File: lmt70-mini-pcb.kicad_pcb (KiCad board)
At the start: 4 copper layers, 7.8 x 8.4 mm, 3 parts, among them P1 CONN_01X04, U1 LMT70

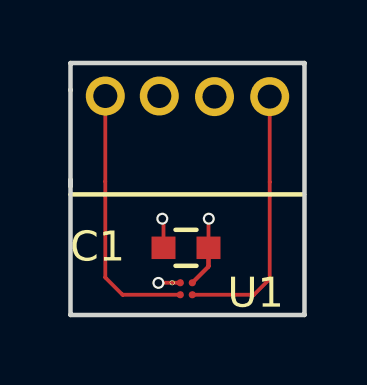
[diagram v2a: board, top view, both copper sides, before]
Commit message: PCB changed for manufacturing with JLCPCB
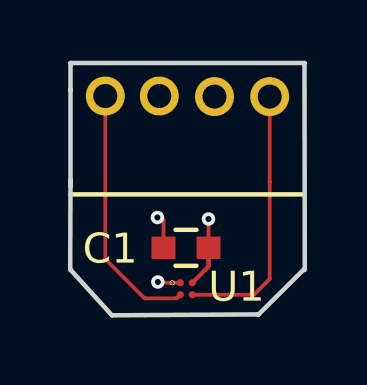
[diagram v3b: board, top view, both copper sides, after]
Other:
- outline, holes or cut-outs redrawn
- net class Default: via_dia 0.4 -> 0.45; via_drill 0.254 -> 0.2
- rule via_min_drill: 0.254 -> 0.2
- rule via_min_size: 0.4 -> 0.45
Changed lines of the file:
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@@
-(kicad_pcb (version 4) (host pcbnew 4.0.5)
+(kicad_pcb (version 20171130) (host pcbnew "(5.0.0-3-g5ebb6b6)")
   (general
-    (links 6)
-    (no_connects 0)
-    (area 146.169667 102.996809 156.290001 113.375001)
     (thickness 1.6)
-    (drawings 7)
-    (tracks 32)
+    (drawings 9)
+    (tracks 39)
     (zones 0)
     (modules 3)
@@
     (segment_width 0.15)
     (edge_width 0.15)
-    (via_size 0.4)
-    (via_drill 0.254)
-    (via_min_size 0.4)
-    (via_min_drill 0.254)
+    (via_size 0.45)
+    (via_drill 0.2)
+    (via_min_size 0.45)
+    (via_min_drill 0.2)
     (uvia_size 0.3)
     (uvia_drill 0.1)
@@
     (visible_elements FFFEFFFF)
     (pcbplotparams
-      (layerselection 0x01008_00000000)
+      (layerselection 0x010a8_ffffffff)
       (usegerberextensions false)
+      (usegerberattributes false)
+      (usegerberadvancedattributes false)
+      (creategerberjobfile false)
       (excludeedgelayer true)
       (linewidth 0.100000)
@@
       (hpglpennumber 1)
       (hpglpenspeed 20)
-      (hpglpendiameter 15)
-      (hpglpenoverlay 2)
+      (hpglpendiameter 15.000000)
       (psnegative false)
       (psa4output false)
@@
       (drillshape 0)
       (scaleselection 1)
-      (outputdirectory ""))
+      (outputdirectory "gerbers/"))
   )
   (net 0 "")
@@
     (clearance 0.127)
     (trace_width 0.127)
-    (via_dia 0.4)
-    (via_drill 0.254)
+    (via_dia 0.45)
+    (via_drill 0.2)
     (uvia_dia 0.3)
     (uvia_drill 0.1)
@@
     (tags "capacitor 0603")
     (attr smd)
-    (fp_text reference C1 (at 2.95 0.04 180) (layer F.SilkS)
+    (fp_text reference C1 (at 2.53 -0.03 180) (layer F.SilkS)
       (effects (font (size 1 1) (thickness 0.15)))
     )
@@
   (module lmt70:LMT70 (layer F.Cu)
     (at 151.659524 112.225)
-    (fp_text reference U1 (at 2.510476 0.335 180) (layer F.SilkS)
+    (fp_text reference U1 (at 1.870476 0.135 180) (layer F.SilkS)
       (effects (font (size 1 1) (thickness 0.15)))
     )
@@
       (net 4 "Net-(P1-Pad4)"))
   )
-  (gr_line (start 148 113.3) (end 148 108.8) (angle 90) (layer Edge.Cuts) (width 0.15))
-  (gr_line (start 155.8 113.3) (end 148 113.3) (angle 90) (layer Edge.Cuts) (width 0.15))
-  (gr_line (start 155.8 104.9) (end 155.8 113.3) (angle 90) (layer Edge.Cuts) (width 0.15))
+  (gr_line (start 154.27 113.28) (end 149.38 113.31) (layer Edge.Cuts) (width 0.15))
+  (gr_line (start 155.79 111.77) (end 154.26 113.29) (layer Edge.Cuts) (width 0.15))
+  (gr_line (start 149.38 113.31) (end 148 111.79) (layer Edge.Cuts) (width 0.15))
+  (gr_line (start 147.99 111.8) (end 148 108.8) (angle 90) (layer Edge.Cuts) (width 0.15))
+  (gr_line (start 155.8 104.9) (end 155.81 111.8) (angle 90) (layer Edge.Cuts) (width 0.15))
   (gr_line (start 148 104.9) (end 155.8 104.9) (angle 90) (layer Edge.Cuts) (width 0.15))
   (gr_line (start 148 105.8) (end 148 104.9) (angle 90) (layer Edge.Cuts) (width 0.15))
@@
   (gr_line (start 147.99 109.28) (end 155.79 109.28) (angle 90) (layer F.SilkS) (width 0.15))
   (segment (start 152.8 106.02) (end 152.8 108.87) (width 0.127) (layer In2.Cu) (net 1))
-  (segment (start 152.6 110.1) (end 152.6 111.684524) (width 0.127) (layer F.Cu) (net 1))
+  (segment (start 152.6 110.1) (end 152.6 110.1) (width 0.127) (layer F.Cu) (net 1))
   (segment (start 152.61 110.09) (end 152.6 110.1) (width 0.127) (layer F.Cu) (net 1))
-  (via (at 152.61 110.09) (size 0.4) (drill 0.254) (layers F.Cu B.Cu) (net 1))
   (segment (start 152.8 109.9) (end 152.61 110.09) (width 0.127) (layer In2.Cu) (net 1))
   (segment (start 152.8 108.87) (end 152.8 109.9) (width 0.127) (layer In2.Cu) (net 1))
@@
   (segment (start 152.6 111.684524) (end 152.059524 112.225) (width 0.127) (layer F.Cu) (net 1))
   (segment (start 152.62 111.08) (end 152.6 111.06) (width 0.127) (layer F.Cu) (net 1))
+  (segment (start 152.6 110.1) (end 152.6 111.684524) (width 0.127) (layer F.Cu) (net 1))
+  (via (at 152.6 110.1) (size 0.45) (drill 0.2) (layers F.Cu B.Cu) (net 1))
   (segment (start 150.956833 108.910359) (end 150.956833 106.003167) (width 0.127) (layer In1.Cu) (net 2))
   (segment (start 150.956833 106.003167) (end 150.96 106) (width 0.127) (layer In1.Cu) (net 2))
-  (segment (start 151.659524 112.225) (end 150.935 112.225) (width 0.127) (layer F.Cu) (net 2))
-  (segment (start 150.79 112.09) (end 150.956833 108.910359) (width 0.127) (layer In1.Cu) (net 2))
   (segment (start 150.956833 108.910359) (end 150.96 108.85) (width 0.127) (layer In1.Cu) (net 2))
-  (segment (start 150.93 112.23) (end 150.79 112.09) (width 0.127) (layer In1.Cu) (net 2))
-  (via (at 150.93 112.23) (size 0.4) (drill 0.254) (layers F.Cu B.Cu) (net 2))
-  (segment (start 150.935 112.225) (end 150.93 112.23) (width 0.127) (layer F.Cu) (net 2))
   (segment (start 150.96 108.85) (end 150.96 109.99) (width 0.127) (layer In1.Cu) (net 2))
   (segment (start 151.1 110.13) (end 151.1 111.06) (width 0.127) (layer F.Cu) (net 2))
   (segment (start 151.06 110.09) (end 151.1 110.13) (width 0.127) (layer F.Cu) (net 2))
-  (via (at 151.06 110.09) (size 0.4) (drill 0.254) (layers F.Cu B.Cu) (net 2))
   (segment (start 150.96 109.99) (end 151.06 110.09) (width 0.127) (layer In1.Cu) (net 2))
   (segment (start 151.11 111.07) (end 151.1 111.06) (width 0.127) (layer F.Cu) (net 2))
-  (segment (start 149.16 106) (end 149.16 108.85) (width 0.127) (layer F.Cu) (net 3))
-  (segment (start 149.735 112.625) (end 149.16 112.05) (width 0.127) (layer F.Cu) (net 3))
-  (segment (start 149.16 112.05) (end 149.16 108.85) (width 0.127) (layer F.Cu) (net 3))
-  (segment (start 149.735 112.625) (end 151.659524 112.625) (width 0.127) (layer F.Cu) (net 3))
+  (segment (start 150.897038 110.05) (end 150.956833 108.910359) (width 0.127) (layer In1.Cu) (net 2))
+  (via (at 150.897038 110.05) (size 0.45) (drill 0.2) (layers F.Cu B.Cu) (net 2))
+  (segment (start 150.935 112.225) (end 150.935 112.225) (width 0.127) (layer F.Cu) (net 2))
+  (segment (start 151.659524 112.225) (end 150.935 112.225) (width 0.127) (layer F.Cu) (net 2))
+  (segment (start 150.91 112.201802) (end 150.91 112.200002) (width 0.127) (layer F.Cu) (net 2))
+  (via (at 150.91 112.200002) (size 0.45) (drill 0.2) (layers F.Cu B.Cu) (net 2))
+  (segment (start 150.935 112.225) (end 150.910002 112.200002) (width 0.127) (layer F.Cu) (net 2))
+  (segment (start 150.910002 112.200002) (end 150.91 112.200002) (width 0.127) (layer F.Cu) (net 2))
+  (segment (start 150.897038 112.18704) (end 150.91 112.200002) (width 0.127) (layer In1.Cu) (net 2))
+  (segment (start 150.93 112.221802) (end 150.91 112.201802) (width 0.127) (layer F.Cu) (net 2))
+  (segment (start 150.93 112.23) (end 150.93 112.221802) (width 0.127) (layer F.Cu) (net 2))
+  (segment (start 150.897038 110.05) (end 150.897038 112.18704) (width 0.127) (layer In1.Cu) (net 2))
+  (segment (start 149.16 106) (end 149.16 111.434944) (width 0.127) (layer F.Cu) (net 3))
+  (segment (start 150.470055 112.744999) (end 151.539525 112.744999) (width 0.127) (layer F.Cu) (net 3))
+  (segment (start 151.539525 112.744999) (end 151.659524 112.625) (width 0.127) (layer F.Cu) (net 3))
+  (segment (start 149.16 111.434944) (end 150.470055 112.744999) (width 0.127) (layer F.Cu) (net 3))
   (segment (start 154.64 106.02) (end 154.64 108.87) (width 0.127) (layer F.Cu) (net 4))
   (segment (start 154.115 112.625) (end 154.64 112.1) (width 0.127) (layer F.Cu) (net 4))
